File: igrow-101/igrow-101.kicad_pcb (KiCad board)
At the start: 2 copper layers, 50.8 x 50.8 mm, 16 parts, among them P1 CONN_02X05, Q1 NPN, U1 NRF51822-MODULE, U2 SHT21

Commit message: WIP
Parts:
- Q1: footprint Housings_SOT-23_SOT-143_TSOT-6:SOT23_Transistor_BC846_Handsoldering_RevB_14Mar2014 -> SMD_Packages:SOT-23
- moved D2 113.6 mm to (175.3, 100.3), turned to 0 degrees
- moved D3 113.4 mm to (175.3, 102.9), turned to 0 degrees
- moved R1 103.6 mm to (171.4, 100.3), turned to 180 degrees
- moved R2 103.4 mm to (171.4, 102.9), turned to 180 degrees
- moved D1 101.5 mm to (170.2, 92.7), turned to 180 degrees
- moved P1 96.6 mm to (177.8, 113.0), turned to 180 degrees
- moved BT1 90.3 mm to (157.5, 85.1)
- moved PIEZO1 83.0 mm to (162.6, 125.7), turned to 180 degrees
- moved R4 83.0 mm to (162.6, 125.7)
- moved R5 82.3 mm to (161.3, 128.3), turned to 180 degrees
- moved D4 81.2 mm to (161.3, 123.2)
- moved R3 77.5 mm to (157.5, 123.2)
- moved Q1 74.0 mm to (153.7, 124.5)
- moved U1 73.4 mm to (148.5, 105.0)
- moved C1 73.1 mm to (143.5, 115.6), turned to 180 degrees
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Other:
- board outline removed

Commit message: Add simulation work and schematic/board WIP
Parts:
- added Q2: NPN, Housings_SOT-23_SOT-143_TSOT-6:SOT-23_Handsoldering, F.Cu at (144.8, 120.7)
- added Q3: NPN, Housings_SOT-23_SOT-143_TSOT-6:SOT-23_Handsoldering, F.Cu at (149.9, 120.7)
- added R10: R, Resistors_SMD:R_0603_HandSoldering, F.Cu at (153.7, 121.3)
- added R11: R, Resistors_SMD:R_0603_HandSoldering, F.Cu at (158.8, 124.5)
- added R6: R, Resistors_SMD:R_0603_HandSoldering, F.Cu at (146.1, 101.6)
- added R7: R, Resistors_SMD:R_0603_HandSoldering, F.Cu at (148.6, 98.4)
- added R8: R, Resistors_SMD:R_0603_HandSoldering, F.Cu at (144.8, 109.9)
- added R9: R, Resistors_SMD:R_0603_HandSoldering, F.Cu at (152.4, 109.9)
- added SW1: SW_PUSH, igrow:SPSTSW, F.Cu at (144.8, 125.7)
- added U3: TL972, Housings_SOIC:SOIC-8_3.9x4.9mm_Pitch1.27mm, F.Cu at (137.8, 111.8)
- C1: footprint SMD_Packages:SMD-0603_c -> Capacitors_SMD:C_0603_HandSoldering
- D1: footprint SMD_Packages:SMD-0805 -> Diodes_SMD:Diode-SMC_Handsoldering
- D2, D3: footprint SMD_Packages:SMD-0805 -> LEDs:LED-0805
- Q1: footprint SMD_Packages:SOT-23 -> Housings_SOT-23_SOT-143_TSOT-6:SOT-23_Handsoldering
- R1, R2, R3, R4, R5: footprint SMD_Packages:SMD-0603_r -> Resistors_SMD:R_0603_HandSoldering
- moved BT1 37.1 mm to (186.7, 108.0), turned to 90 degrees
- moved D1 34.9 mm to (176.5, 127.0)
- moved D2 33.5 mm to (144.8, 114.3), turned to 270 degrees
- moved PIEZO1 33.2 mm to (139.7, 101.6), turned to 90 degrees
- moved D4 33.2 mm to (137.2, 100.3), turned to 270 degrees
- moved R5 32.4 mm to (142.9, 101.6), turned to 90 degrees
- moved R1 28.3 mm to (163.8, 127.6), turned to 0 degrees
- moved R2 28.3 mm to (163.8, 130.2), turned to 0 degrees
- moved R4 25.6 mm to (152.4, 102.2), turned to 270 degrees
- moved D3 25.6 mm to (152.4, 114.3), turned to 270 degrees
- moved C1 19.7 mm to (148.6, 96.5), turned to 0 degrees
- moved Q1 14.5 mm to (139.7, 120.7)
- moved P1 14.4 mm to (188.0, 123.2), turned to 0 degrees
- moved U2 9.52 mm to (149.9, 104.8), turned to 180 degrees
- moved U1 7.72 mm to (156.2, 105.4)
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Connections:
- D2 pad 2: GND -> Net-(D2-Pad2)
- D3 pad 2: GND -> Net-(D3-Pad2)
- R1 pad 1: Net-(D2-Pad1) -> Net-(Q2-Pad2)
- R2 pad 1: Net-(D3-Pad1) -> Net-(Q3-Pad2)
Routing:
- net Net-(U1-Pad1): track 0.00 -> 8.41 mm
- net Net-(U1-Pad2): track 0.00 -> 8.41 mm
- net (no net): track 0.00 -> 6.50 mm

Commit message: Post autorouting
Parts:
- BT1: footprint guan:BAT-BK912 -> igrow:CR2032_THRUHOLE
- PIEZO1: footprint Resistors_ThroughHole:Resistor_Horizontal_RM10mm -> Resistors_SMD:R_0805_HandSoldering
- moved D1 37.1 mm to (143.5, 110.0)
- moved BT1 34.0 mm to (152.9, 112.0), turned to 270 degrees
- moved D4 21.1 mm to (136.7, 121.4), turned to 90 degrees
- moved R5 18.0 mm to (142.2, 119.6), turned to 270 degrees
- moved PIEZO1 18.0 mm to (139.4, 119.6), turned to 270 degrees
- moved P1 16.5 mm to (172.7, 129.5), turned to 180 degrees
- moved R4 16.0 mm to (142.2, 114.6)
- moved R10 10.6 mm to (163.8, 124.5), turned to 180 degrees
- moved Q1 10.6 mm to (148.3, 126.7)
- moved Q2 10.6 mm to (153.4, 126.7)
- moved Q3 10.6 mm to (158.5, 126.7)
- moved U3 10.3 mm to (139.7, 101.6)
- moved C1 9.12 mm to (146.6, 105.4), turned to 90 degrees
- moved D3 7.03 mm to (147.8, 119.6)
- moved R9 6.96 mm to (148.1, 115.3)
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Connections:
- U1 pad 20: Net-(U1-Pad20) -> Net-(R2-Pad2)
- U1 pad 21: Net-(U1-Pad21) -> Net-(R1-Pad2)
- U1 pad 33: Net-(R2-Pad2) -> Net-(U1-Pad33)
- U1 pad 36: Net-(R1-Pad2) -> Net-(U1-Pad36)
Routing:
- net GND: track 0.00 -> 139.6 mm
- net VCC: track 0.00 -> 64.2 mm
- net Net-(R10-Pad2): track 0.00 -> 26.4 mm
- net Net-(Q1-Pad2): track 0.00 -> 20.5 mm
- net Net-(P1-Pad2): track 0.00 -> 18.9 mm
- net Net-(P1-Pad4): track 0.00 -> 17.6 mm
- net Net-(D4-Pad1): track 0.00 -> 16.7 mm
- net Net-(D3-Pad2): track 0.00 -> 12.6 mm
- net Net-(R1-Pad2): track 0.00 -> 11.9 mm
- net Net-(D2-Pad2): track 0.00 -> 10.2 mm
- net Net-(R2-Pad2): track 0.00 -> 9.55 mm
- net Net-(Q2-Pad2): track 0.00 -> 9.00 mm
- net Net-(D4-Pad2): track 0.00 -> 8.83 mm
- net Net-(R3-Pad2): track 0.00 -> 7.25 mm
- net (no net): track 6.50 -> 0.00 mm
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
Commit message: First attempt at cooking a board...
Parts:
- added REF**: MountingHole_3mm, Mounting_Holes:MountingHole_3mm, F.Cu at (177.8, 96.5)
- added REF**: MountingHole_3mm, Mounting_Holes:MountingHole_3mm, F.Cu at (134.6, 96.5)
- added REF**: MountingHole_3mm, Mounting_Holes:MountingHole_3mm, F.Cu at (134.6, 129.5)
- added REF**: MountingHole_3mm, Mounting_Holes:MountingHole_3mm, F.Cu at (177.8, 129.5)
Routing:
- added copper zone on F.Cu, net GND
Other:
- board outline added: 49.8 x 39.5 mm
- board text added: "iGrow 101 nRF51822 (c) 2015 Argusat Limited"
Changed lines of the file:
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@@
     (links 49)
     (no_connects 0)
-    (area 130.810857 94.02 177.333857 134.578999)
+    (area 128.077474 91.3405 186.344046 135.57026)
     (thickness 1.6)
-    (drawings 1)
+    (drawings 6)
     (tracks 201)
     (zones 0)
-    (modules 26)
+    (modules 30)
     (nets 59)
   )
   (page A4)
+  (title_block
+    (title "iGrow Nordic nRF51822 Node")
+    (date "Monday, 06 April 2015")
+    (rev 101)
+    (company "Argusat Limited")
+    (comment 1 "Research and Development ")
+  )
   (layers
     (0 F.Cu signal)
@@
       (drillshape 1)
       (scaleselection 1)
-      (outputdirectory ""))
+      (outputdirectory svg/))
   )
   (net 0 "")
@@
     (add_net VTG)
   )
+  (module Mounting_Holes:MountingHole_3mm (layer F.Cu)
+    (at 177.8 96.52)
+    (descr "Mounting hole, Befestigungsbohrung, 3mm, No Annular, Kein Restring,")
+    (tags "Mounting hole, Befestigungsbohrung, 3mm, No Annular, Kein Restring,")
+    (fp_text reference REF** (at 0 -4.0005) (layer F.SilkS)
+      (effects (font (size 1 1) (thickness 0.15)))
+    )
+    (fp_text value MountingHole_3mm (at 1.00076 5.00126) (layer F.Fab)
+      (effects (font (size 1 1) (thickness 0.15)))
+    )
+    (fp_circle (center 0 0) (end 3 0) (layer Cmts.User) (width 0.381))
+    (pad 1 thru_hole circle (at 0 0) (size 3 3) (drill 3) (layers))
+  )
   (module Capacitors_SMD:C_0603_HandSoldering (layer F.Cu)
     (at 146.558 105.41 90)
@@
     )
   )
-  (target plus (at 133.35 96.52) (size 5) (width 0.15) (layer Edge.Cuts))
+  (module Mounting_Holes:MountingHole_3mm (layer F.Cu)
+    (at 134.62 96.52)
+    (descr "Mounting hole, Befestigungsbohrung, 3mm, No Annular, Kein Restring,")
+    (tags "Mounting hole, Befestigungsbohrung, 3mm, No Annular, Kein Restring,")
+    (fp_text reference REF** (at 0 -4.0005) (layer F.SilkS)
+      (effects (font (size 1 1) (thickness 0.15)))
+    )
+    (fp_text value MountingHole_3mm (at 1.00076 5.00126) (layer F.Fab)
+      (effects (font (size 1 1) (thickness 0.15)))
+    )
+    (fp_circle (center 0 0) (end 3 0) (layer Cmts.User) (width 0.381))
+    (pad 1 thru_hole circle (at 0 0) (size 3 3) (drill 3) (layers))
+  )
+  (module Mounting_Holes:MountingHole_3mm (layer F.Cu)
+    (at 134.62 129.54)
+    (descr "Mounting hole, Befestigungsbohrung, 3mm, No Annular, Kein Restring,")
+    (tags "Mounting hole, Befestigungsbohrung, 3mm, No Annular, Kein Restring,")
+    (fp_text reference REF** (at 0 -4.0005) (layer F.SilkS)
+      (effects (font (size 1 1) (thickness 0.15)))
+    )
+    (fp_text value MountingHole_3mm (at 1.00076 5.00126) (layer F.Fab)
+      (effects (font (size 1 1) (thickness 0.15)))
+    )
+    (fp_circle (center 0 0) (end 3 0) (layer Cmts.User) (width 0.381))
+    (pad 1 thru_hole circle (at 0 0) (size 3 3) (drill 3) (layers))
+  )
+  (module Mounting_Holes:MountingHole_3mm (layer F.Cu)
+    (at 177.8 129.54)
+    (descr "Mounting hole, Befestigungsbohrung, 3mm, No Annular, Kein Restring,")
+    (tags "Mounting hole, Befestigungsbohrung, 3mm, No Annular, Kein Restring,")
+    (fp_text reference REF** (at 0 -4.0005) (layer F.SilkS)
+      (effects (font (size 1 1) (thickness 0.15)))
+    )
+    (fp_text value MountingHole_3mm (at 1.00076 5.00126) (layer F.Fab)
+      (effects (font (size 1 1) (thickness 0.15)))
+    )
+    (fp_circle (center 0 0) (end 3 0) (layer Cmts.User) (width 0.381))
+    (pad 1 thru_hole circle (at 0 0) (size 3 3) (drill 3) (layers))
+  )
+  (gr_text "iGrow 101 nRF51822\n(c) 2015 Argusat Limited" (at 150.241 116.459 90) (layer F.Cu)
+    (effects (font (size 0.3 0.3) (thickness 0.07)))
+  )
+  (gr_line (start 181.102 132.715) (end 131.318 132.715) (angle 90) (layer Edge.Cuts) (width 0.15))
+  (gr_line (start 181.102 93.218) (end 181.102 132.715) (angle 90) (layer Edge.Cuts) (width 0.15))
+  (gr_line (start 131.318 93.218) (end 181.102 93.218) (angle 90) (layer Edge.Cuts) (width 0.15))
+  (gr_line (start 131.318 132.715) (end 131.318 93.218) (angle 90) (layer Edge.Cuts) (width 0.15))
+  (target plus (at 134.62 96.52) (size 5) (width 0.15) (layer Edge.Cuts))
   (segment (start 149.368 104.14) (end 149.368 103.4587) (width 0.254) (layer F.Cu) (net 2))
   (segment (start 171.1387 127.6226) (end 171.1387 127) (width 0.254) (layer F.Cu) (net 2))
@@
   (segment (start 150.368 107.2213) (end 155.6687 107.2213) (width 0.254) (layer F.Cu) (net 27))
   (segment (start 150.368 106.54) (end 150.368 107.2213) (width 0.254) (layer F.Cu) (net 27))
+  (zone (net 2) (net_name GND) (layer F.Cu) (hatch edge 0.508)
+    (connect_pads (clearance 0.508))
+    (min_thickness 0.254)
+    (fill yes (arc_segments 16) (thermal_gap 0.508) (thermal_bridge_width 0.508))
+    (polygon
+      (pts
+        (xy 181.102 132.715) (xy 131.318 132.715) (xy 131.318 93.218) (xy 181.102 93.218)
+      )
+    )
+  )
 )

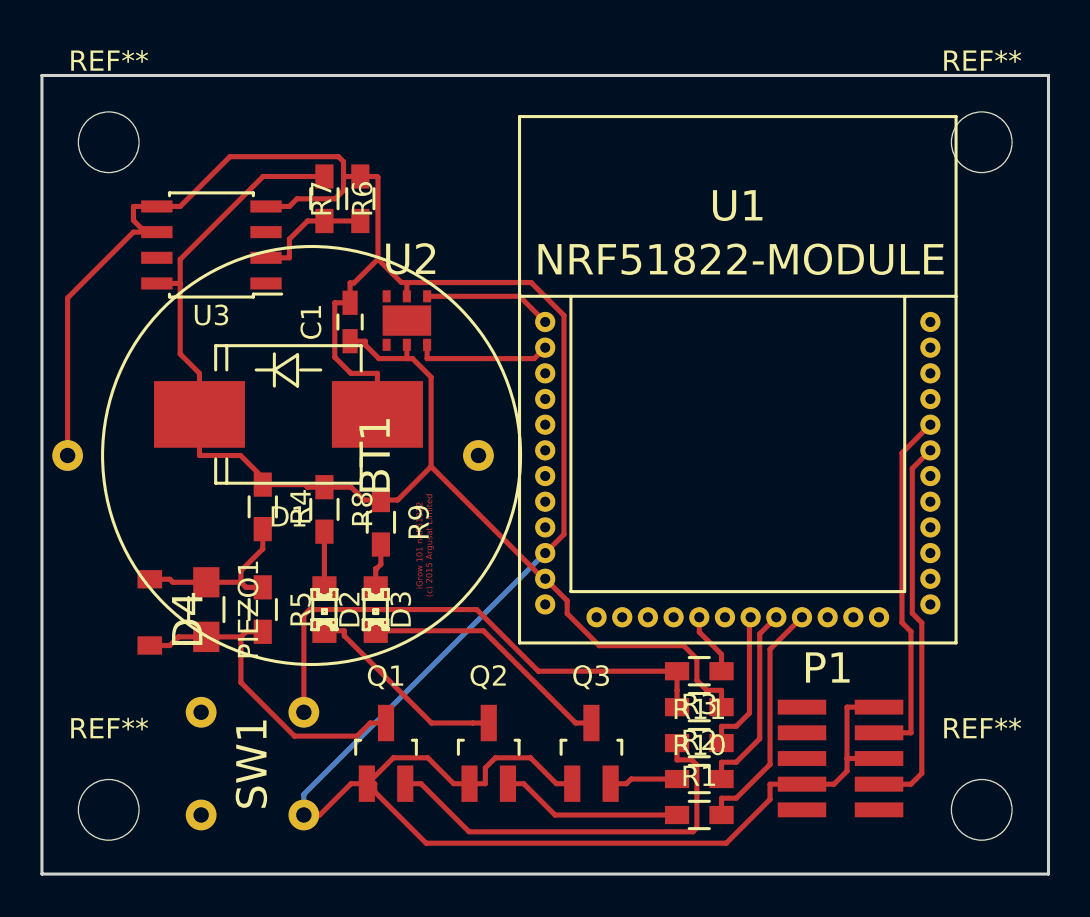
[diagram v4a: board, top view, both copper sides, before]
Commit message: Flip module to other side, correct header pinout and make the module pads bigger
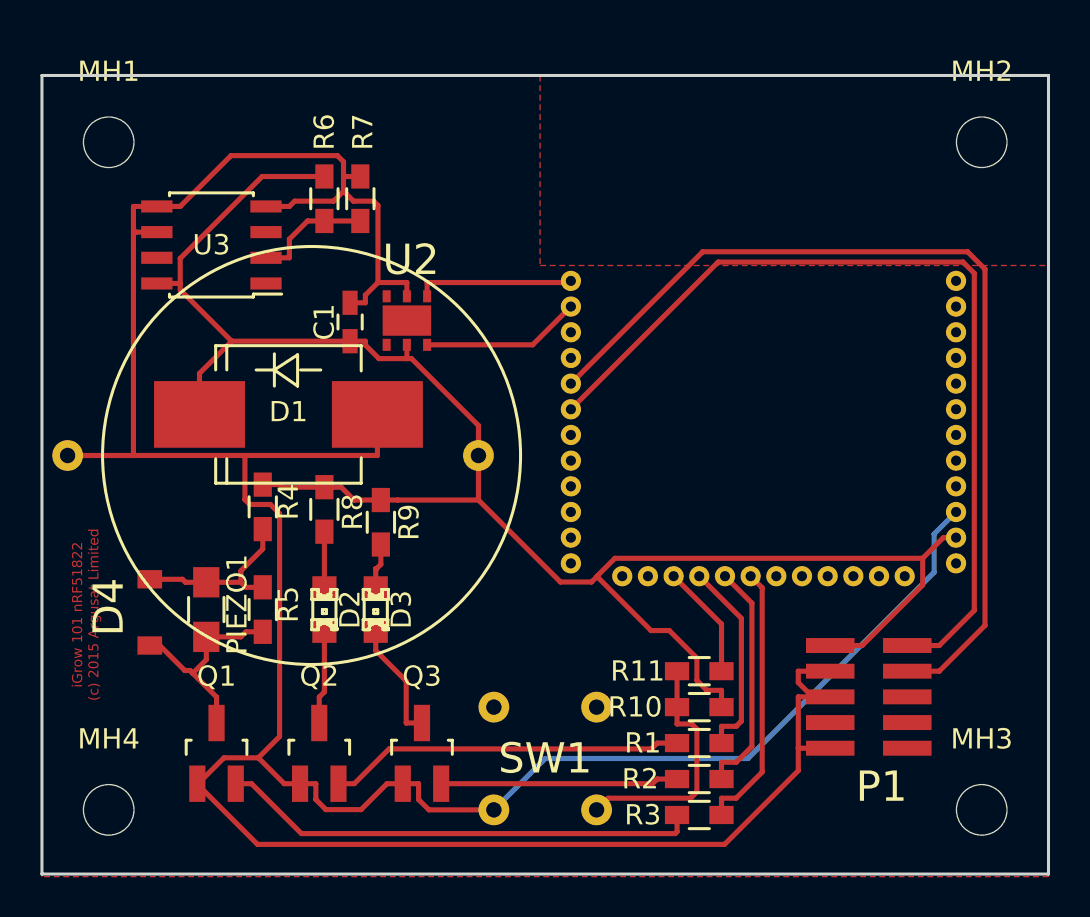
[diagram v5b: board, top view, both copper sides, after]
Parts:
- removed REF** (x4): MountingHole_3mm, Mounting_Holes:MountingHole_3mm
- added MH1: MountingHole_2-5mm, Mounting_Holes:MountingHole_2-5mm, F.Cu at (134.6, 96.5)
- added MH2: MountingHole_2-5mm, Mounting_Holes:MountingHole_2-5mm, F.Cu at (177.8, 96.5)
- added MH3: MountingHole_2-5mm, Mounting_Holes:MountingHole_2-5mm, F.Cu at (177.8, 129.5)
- added MH4: MountingHole_2-5mm, Mounting_Holes:MountingHole_2-5mm, F.Cu at (134.6, 129.5)
- U1: moved to B.Cu
- moved U1 20.4 mm to (176.5, 103.4), turned to 180 degrees
- moved SW1 15.3 mm to (158.8, 129.5), turned to 180 degrees
- moved P1 8.48 mm to (170.3, 121.4), turned to 0 degrees
- moved Q1 8.38 mm to (140.0, 126.7)
- moved Q2 8.38 mm to (145.0, 126.7)
- moved Q3 8.38 mm to (150.1, 126.7)
- moved R1 3.56 mm to (163.8, 126.2)
- moved R3 3.56 mm to (163.8, 129.8)
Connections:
- BT1 pad 1: Net-(BT1-Pad1) -> VCC
- P1 pad 1: VTG -> VCC
- U1 pad 17: Net-(R11-Pad1) -> Net-(U1-Pad17)
- U1 pad 22: Net-(U1-Pad22) -> Net-(R11-Pad1)
- U2 pad 1: Net-(U1-Pad1) -> Net-(U1-Pad36)
- U2 pad 6: Net-(U1-Pad2) -> Net-(U1-Pad35)
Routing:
- net Net-(P1-Pad4): track 17.6 -> 45.9 mm
- net VCC: track 64.2 -> 92.1 mm
- net GND: track 139.6 -> 166.3 mm
- net Net-(P1-Pad2): track 18.9 -> 43.9 mm
- net Net-(R10-Pad2): track 26.4 -> 12.1 mm
- net Net-(Q2-Pad2): track 9.00 -> 17.6 mm
- net Net-(Q3-Pad2): track 3.38 -> 11.8 mm
- net Net-(U1-Pad35): track 0.00 -> 7.90 mm
- net Net-(U1-Pad36): track 0.00 -> 7.83 mm
- net Net-(U1-Pad2): track 6.75 -> 0.00 mm
- net Net-(D3-Pad2): track 12.6 -> 5.97 mm
- net Net-(U1-Pad1): track 6.37 -> 0.00 mm
- net Net-(R3-Pad2): track 7.25 -> 13.3 mm
- net Net-(D4-Pad1): track 16.7 -> 10.6 mm
- net Net-(D2-Pad2): track 10.2 -> 4.67 mm
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
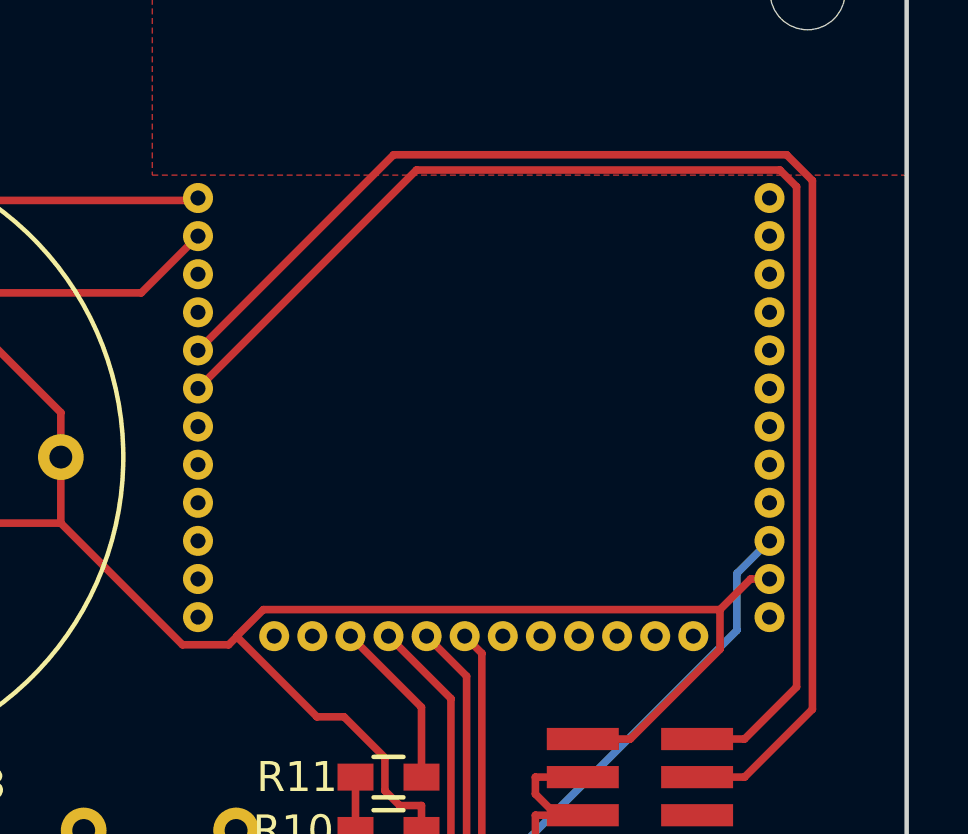
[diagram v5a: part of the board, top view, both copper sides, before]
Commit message: Make module copper pads a bit larger
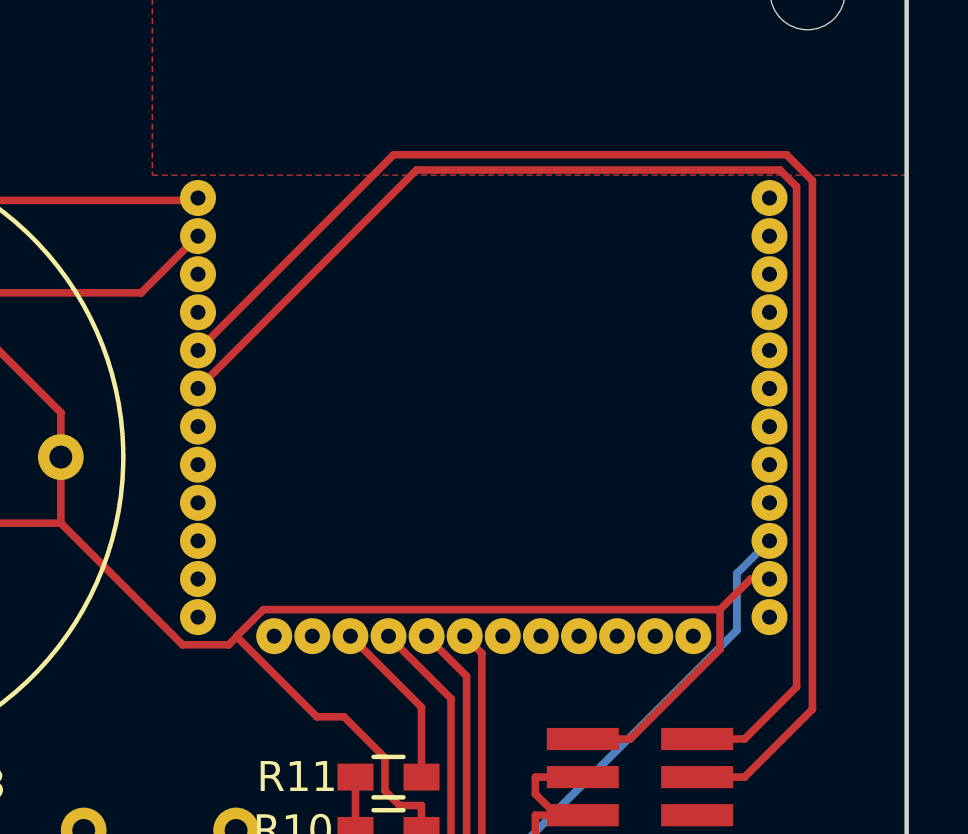
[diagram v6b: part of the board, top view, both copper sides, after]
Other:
- net class Default: trace_width 0.254 -> 0.327
- rule trace_min: 0.254 -> 0.327
